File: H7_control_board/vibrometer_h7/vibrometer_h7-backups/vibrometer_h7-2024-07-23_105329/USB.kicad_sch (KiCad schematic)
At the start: 11 parts, among them J1 USB_C_Receptacle_USB2.0_16P, U2 USBLC6-2SC6, U3 AZ1117-3.3

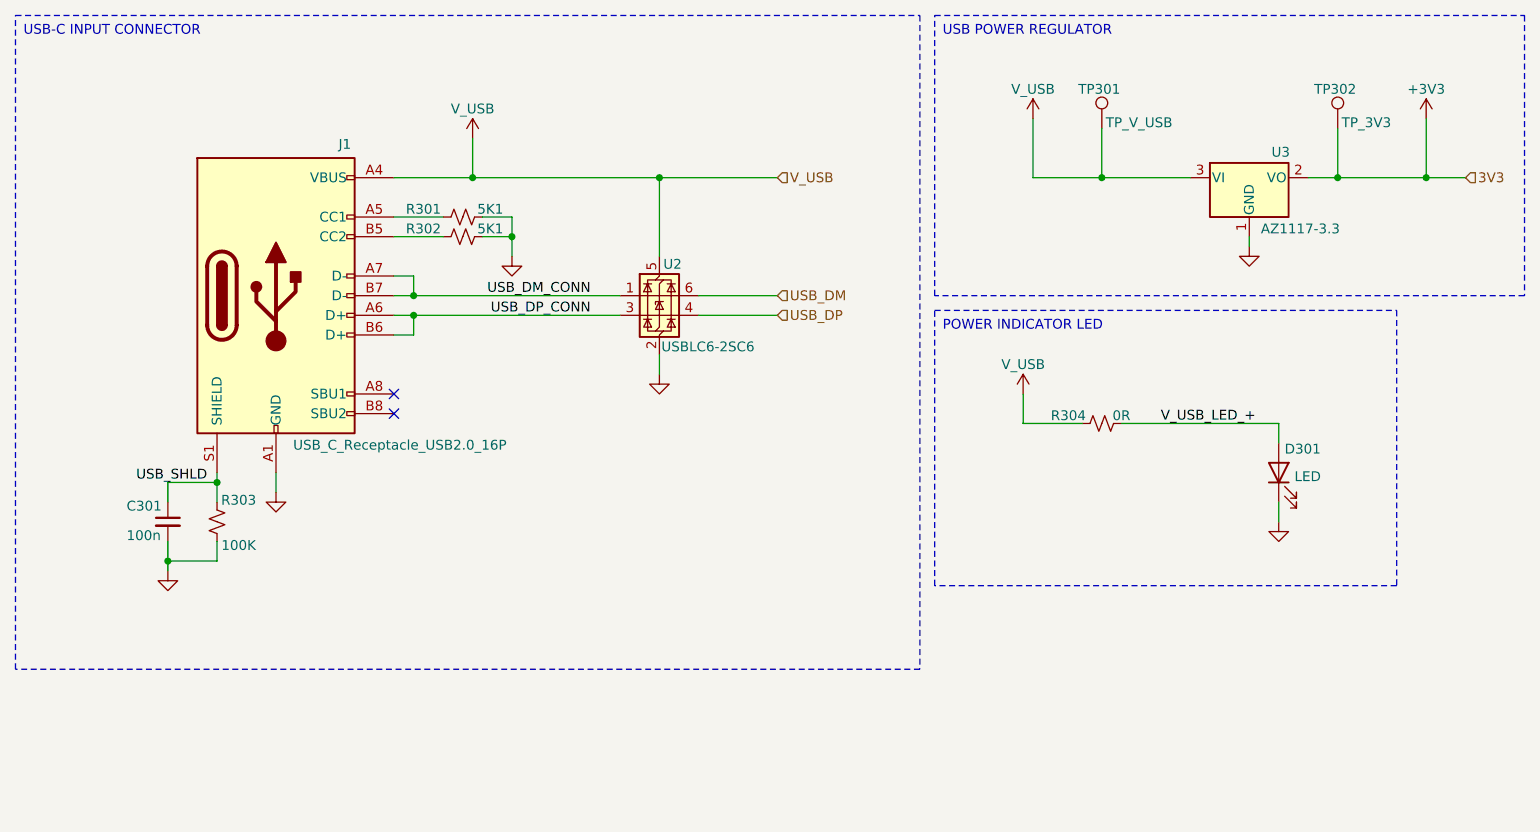
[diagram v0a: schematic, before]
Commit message: added UI leds to schematic
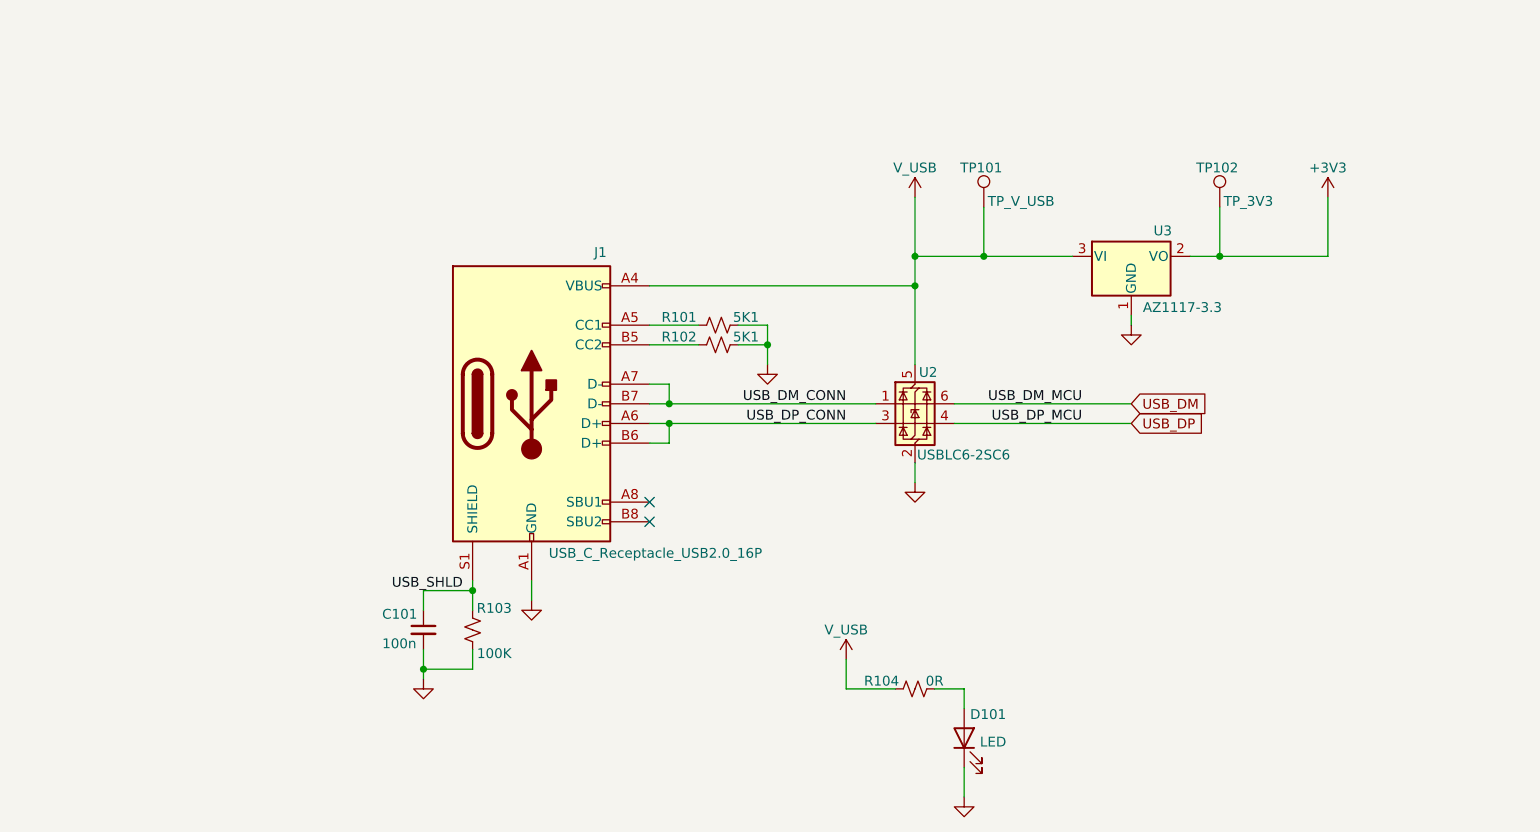
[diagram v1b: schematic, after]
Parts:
- renumbered C301 to C101, D301 to D101, R301 to R101, R302 to R102, R303 to R103, R304 to R104, TP301 to TP101, TP302 to TP102
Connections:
- net V_USB_LED_+: no longer names the net of D101.2 (A), R104.2
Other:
- moved on the sheet: C101, D101, J1, R101, R102, R103, R104, TP101, TP102, U2, U3
